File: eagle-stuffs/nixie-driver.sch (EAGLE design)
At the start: 65 parts, among them IC1 74141N/K155ID1, IC2 74LS595N, IC3 TPS562209, IC4 NE555, Q1 MPSA92, Q10 2N2222, Q11 IRF840, Q12 2N2222, Q2 MPSA92, Q3 MPSA92, Q4 MPSA92, Q5 MPSA42, Q6 MPSA42, Q7 MPSA42, Q8 MPSA42, Q9 PN2907

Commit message: Updated something
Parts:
- R11: value 27 -> 56
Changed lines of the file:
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@@
 <part name="R9" library="resistor" deviceset="R-US_" device="0207/10" value="10k"/>
 <part name="R10" library="resistor" deviceset="R-US_" device="0207/10" value="10k"/>
-<part name="R11" library="resistor" deviceset="R-US_" device="0207/10" value="27"/>
+<part name="R11" library="resistor" deviceset="R-US_" device="0207/10" value="56"/>
 <part name="R12" library="resistor" deviceset="R-US_" device="0207/10" value="10k"/>
 <part name="R13" library="resistor" deviceset="R-US_" device="0207/10" value="15k"/>

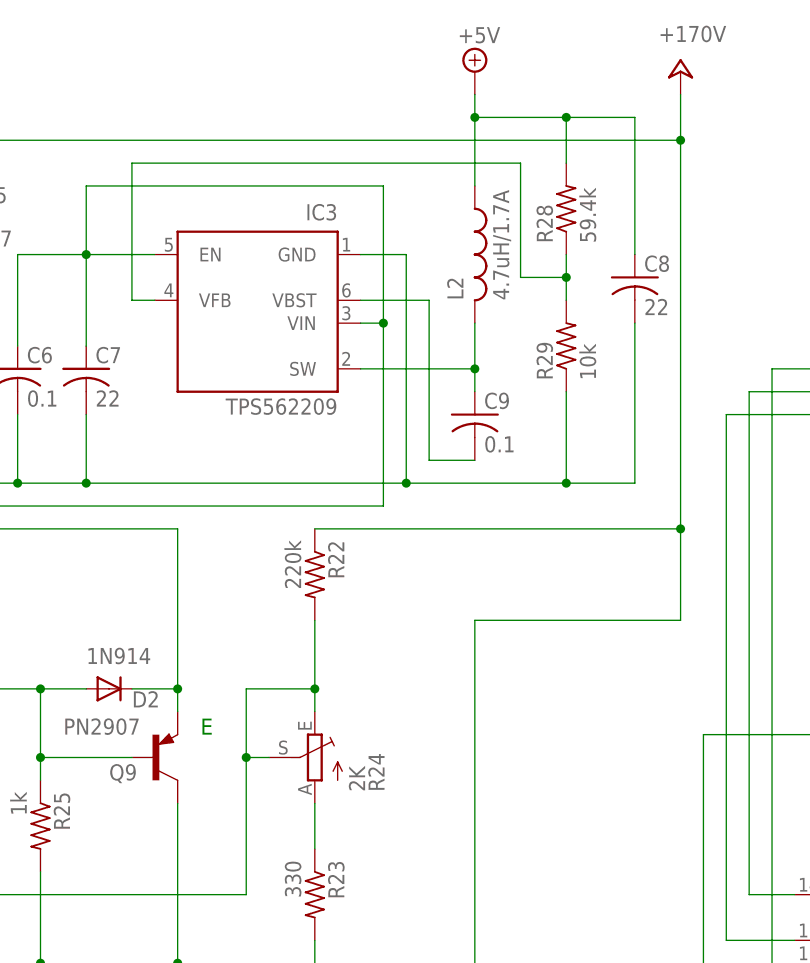
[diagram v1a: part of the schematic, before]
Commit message: Layout adjustement
Adjusted some physical component size & layout
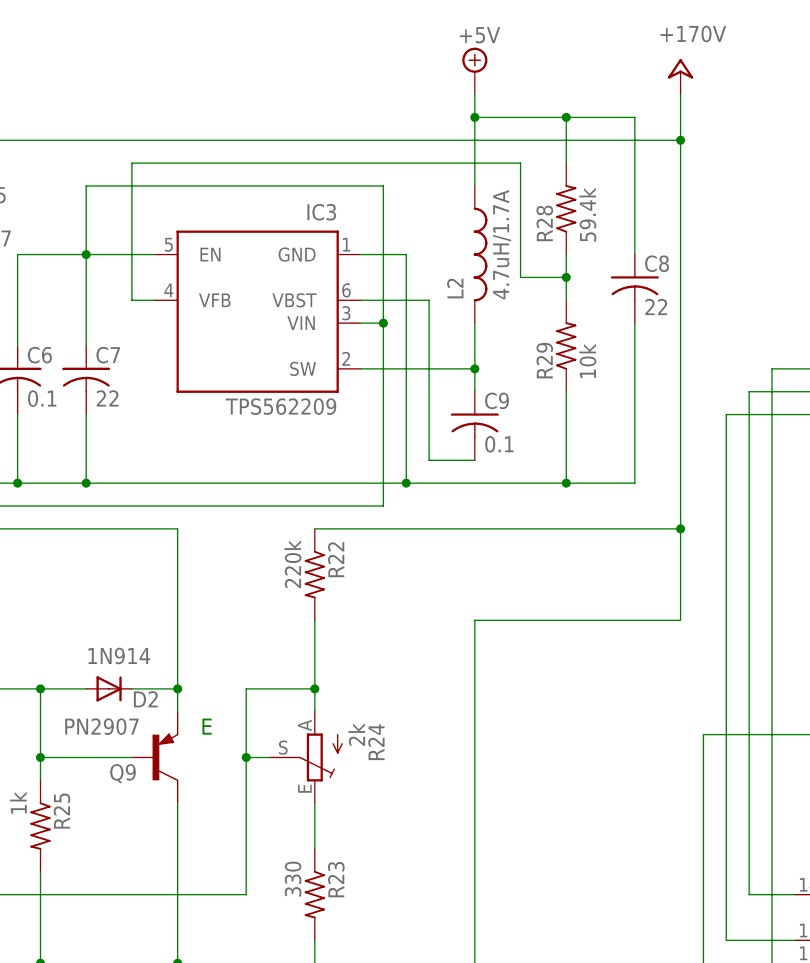
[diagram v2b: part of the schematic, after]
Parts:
- L2: device resistor:L-US0207/10 -> resistor:L-US0207/12
- R24: value 2K -> 2k; device pot:TRIM_EU-CT6 -> pot:TRIM_EU-CA6V
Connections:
- net N$64: now also R24.A; no longer R24.E
- net N$65: now also R24.E; no longer R24.A
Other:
- note added: "Capacitor value in uF in not noted, C4/C5 300v rated"
- note removed: "Capacitor value in uF in not noted"
- moved on the sheet: R24
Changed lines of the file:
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@@
 <part name="R22" library="resistor" deviceset="R-US_" device="0207/10" value="220k"/>
 <part name="R23" library="resistor" deviceset="R-US_" device="0207/10" value="330"/>
-<part name="R24" library="pot" deviceset="TRIM_EU-" device="CT6" value="2K"/>
 <part name="D2" library="diode" deviceset="1N4004" device="" value="1N914"/>
 <part name="Q9" library="transistor-pnp" deviceset="2N4126*" device="" value="PN2907"/>
@@
 <part name="IC3" library="texas" deviceset="TPS6107*" device="DDC" technology="0" value="TPS562209"/>
 <part name="R21" library="resistor" deviceset="R-US_" device="0207/10" value="2.2k"/>
-<part name="L2" library="resistor" deviceset="L-US" device="0207/10" value="4.7uH/1.7A"/>
 <part name="P+1" library="supply1" deviceset="+24V" device="" value="+170V"/>
 <part name="C1" library="rcl" deviceset="CPOL-US" device="E2,5-6E" value="100"/>
@@
 <part name="R29" library="resistor" deviceset="R-US_" device="0204/2V" value="10k"/>
 <part name="C6" library="rcl" deviceset="C-US" device="050-024X044" value="0.1"/>
+<part name="R24" library="pot" deviceset="TRIM_EU-" device="CA6V" value="2k"/>
+<part name="L2" library="resistor" deviceset="L-US" device="0207/12" value="4.7uH/1.7A"/>
 </parts>
 <sheets>
@@
 <wire x1="144.78" y1="99.06" x2="7.62" y2="99.06" width="0.1524" layer="98" style="shortdash"/>
 <wire x1="7.62" y1="99.06" x2="7.62" y2="203.2" width="0.1524" layer="98" style="shortdash"/>
-<text x="27.94" y="205.74" size="1.778" layer="98">Power supply (+5v / 500mA, +170v / 6 mA)</text>
+<text x="38.1" y="208.28" size="1.778" layer="98">Power supply (+5v / 500mA, +170v / 6 mA)</text>
 <text x="223.52" y="45.72" size="1.778" layer="98">Cathode drivers &amp; Ambient led</text>
 <wire x1="147.32" y1="134.62" x2="269.24" y2="134.62" width="0.1524" layer="98" style="shortdash"/>
@@
 <text x="175.26" y="25.4" size="2.54" layer="98" font="fixed">Project:</text>
 <text x="193.04" y="25.4" size="2.54" layer="98" font="fixed">Y.A.N.C. (Yet Another Nixie Clock)</text>
-<text x="83.82" y="200.66" size="1.778" layer="98">Capacitor value in uF in not noted</text>
+<text x="38.1" y="205.74" size="1.778" layer="98">Capacitor value in uF in not noted, C4/C5 300v rated</text>
 <text x="175.26" y="7.62" size="2.54" layer="98" font="fixed">Licensed under CERN OHL v.1.2 or later</text>
 </plain>
@@
 <attribute name="VALUE" x="118.618" y="118.11" size="1.778" layer="96" rot="R270"/>
 </instance>
-<instance part="R24" gate="1" x="121.92" y="129.54" smashed="yes" rot="MR0">
-<attribute name="NAME" x="127.889" y="125.73" size="1.778" layer="95" rot="MR90"/>
-<attribute name="VALUE" x="125.73" y="125.73" size="1.778" layer="96" rot="MR90"/>
-</instance>
 <instance part="D2" gate="1" x="99.06" y="137.16" smashed="yes">
 <attribute name="NAME" x="101.6" y="135.1026" size="1.778" layer="95"/>
@@
 <attribute name="NAME" x="57.3786" y="194.31" size="1.778" layer="95" rot="R270"/>
 <attribute name="VALUE" x="52.578" y="194.31" size="1.778" layer="96" rot="R270"/>
-</instance>
-<instance part="L2" gate="G$1" x="139.7" y="185.42" smashed="yes">
-<attribute name="NAME" x="138.43" y="180.34" size="1.778" layer="95" rot="R90"/>
-<attribute name="VALUE" x="143.51" y="180.34" size="1.778" layer="96" rot="R90"/>
 </instance>
 <instance part="P+1" gate="1" x="162.56" y="205.74" smashed="yes">
@@
 <instance part="R29" gate="G$1" x="149.86" y="175.26" rot="R90"/>
 <instance part="C6" gate="G$1" x="88.9" y="172.72"/>
+<instance part="R24" gate="1" x="121.92" y="129.54" rot="R180"/>
+<instance part="L2" gate="G$1" x="139.7" y="185.42"/>
 </instances>
 <busses>
@@
 <wire x1="149.86" y1="200.66" x2="149.86" y2="195.58" width="0.1524" layer="91"/>
 <junction x="139.7" y="200.66"/>
-<pinref part="L2" gate="G$1" pin="1"/>
 <wire x1="149.86" y1="200.66" x2="157.48" y2="200.66" width="0.1524" layer="91"/>
 <wire x1="157.48" y1="200.66" x2="157.48" y2="185.42" width="0.1524" layer="91"/>
@@
 <pinref part="C8" gate="G$1" pin="1"/>
 <pinref part="R28" gate="G$1" pin="2"/>
+<pinref part="L2" gate="G$1" pin="1"/>
 </segment>
 <segment>
@@
 <wire x1="73.66" y1="114.3" x2="114.3" y2="114.3" width="0.1524" layer="91"/>
 <wire x1="114.3" y1="114.3" x2="114.3" y2="129.54" width="0.1524" layer="91"/>
-<pinref part="R24" gate="1" pin="S"/>
 <wire x1="114.3" y1="129.54" x2="116.84" y2="129.54" width="0.1524" layer="91"/>
 <wire x1="114.3" y1="137.16" x2="114.3" y2="129.54" width="0.1524" layer="91"/>
 <junction x="114.3" y="129.54"/>
-<pinref part="R24" gate="1" pin="E"/>
 <pinref part="R22" gate="G$1" pin="2"/>
 <wire x1="121.92" y1="134.62" x2="121.92" y2="137.16" width="0.1524" layer="91"/>
@@
 <junction x="121.92" y="137.16"/>
 <pinref part="Q10" gate="G$1" pin="B"/>
+<pinref part="R24" gate="1" pin="A"/>
+<pinref part="R24" gate="1" pin="S"/>
 </segment>
 </net>
 <net name="N$65" class="0">
 <segment>
-<pinref part="R24" gate="1" pin="A"/>
 <pinref part="R23" gate="G$1" pin="1"/>
 <wire x1="121.92" y1="119.38" x2="121.92" y2="124.46" width="0.1524" layer="91"/>
+<pinref part="R24" gate="1" pin="E"/>
 </segment>
 </net>
@@
 <net name="SW" class="0">
 <segment>
-<pinref part="L2" gate="G$1" pin="2"/>
 <pinref part="C9" gate="G$1" pin="1"/>
 <wire x1="139.7" y1="170.18" x2="139.7" y2="172.72" width="0.1524" layer="91"/>
@@
 <wire x1="127" y1="172.72" x2="139.7" y2="172.72" width="0.1524" layer="91"/>
 <junction x="139.7" y="172.72"/>
-</segment>
-</net>
+<pinref part="L2" gate="G$1" pin="2"/>
+</segment>
+</net>

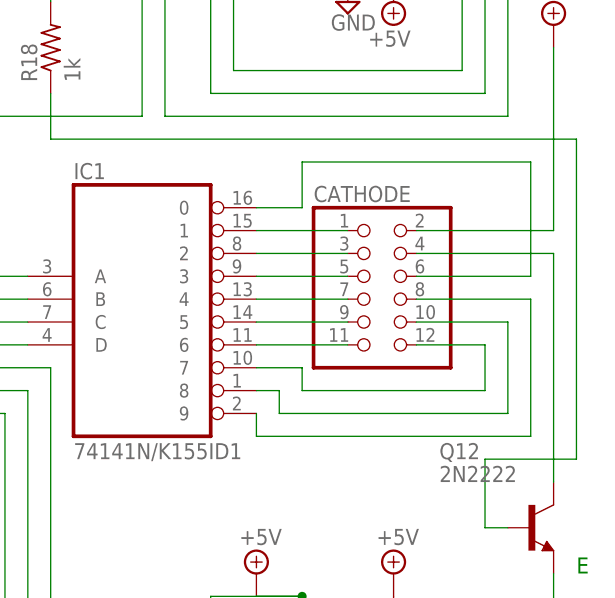
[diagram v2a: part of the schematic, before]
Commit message: Mirror cathod connector
Corrected major layout error!!! Needed to mirror cathod connector since
it mounted on bottom layer on lamp board and not on this board. Blowed
up my Pi this morning for the maiden test of the board :-(
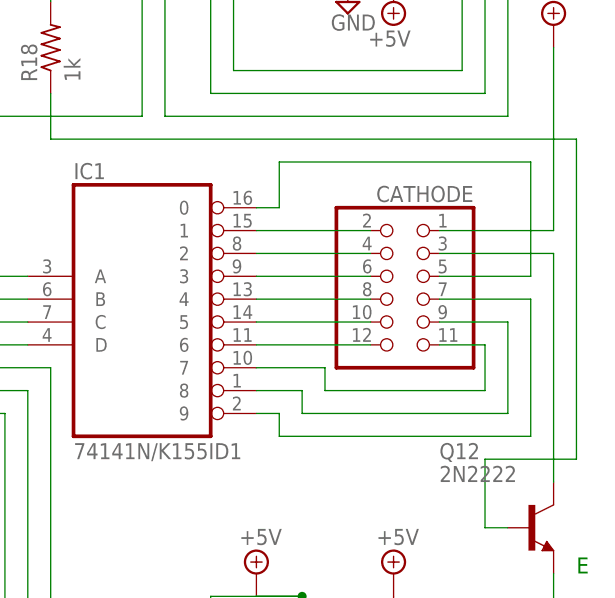
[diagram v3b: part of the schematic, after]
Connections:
- net +5V: now also CATHODE.1; no longer CATHODE.2
- net N$10: now also CATHODE.7; no longer CATHODE.8
- net N$11: now also CATHODE.5; no longer CATHODE.6
- net N$2: now also CATHODE.2; no longer CATHODE.1
- net N$3: now also CATHODE.4; no longer CATHODE.3
- net N$4: now also CATHODE.6; no longer CATHODE.5
- net N$45: now also CATHODE.3; no longer CATHODE.4
- net N$5: now also CATHODE.8; no longer CATHODE.7
- net N$6: now also CATHODE.10; no longer CATHODE.9
- net N$7: now also CATHODE.12; no longer CATHODE.11
- net N$8: now also CATHODE.11; no longer CATHODE.12
- net N$9: now also CATHODE.9; no longer CATHODE.10
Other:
- moved on the sheet: CATHODE
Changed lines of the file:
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@@
 <instance part="SUPPLY8" gate="+5V" x="231.14" y="81.28"/>
 <instance part="SUPPLY9" gate="+5V" x="246.38" y="81.28"/>
-<instance part="CATHODE" gate="A" x="243.84" y="114.3"/>
+<instance part="CATHODE" gate="A" x="248.92" y="114.3" rot="MR0"/>
 <instance part="PI" gate="A" x="223.52" y="157.48" rot="R270"/>
 <instance part="SUPPLY10" gate="GND" x="264.16" y="55.88"/>
@@
 </segment>
 <segment>
-<pinref part="CATHODE" gate="A" pin="2"/>
-<wire x1="248.92" y1="119.38" x2="264.16" y2="119.38" width="0.1524" layer="91"/>
 <pinref part="SUPPLY14" gate="+5V" pin="+5V"/>
 <wire x1="264.16" y1="139.7" x2="264.16" y2="119.38" width="0.1524" layer="91"/>
+<pinref part="CATHODE" gate="A" pin="1"/>
+<wire x1="264.16" y1="119.38" x2="251.46" y2="119.38" width="0.1524" layer="91"/>
 </segment>
 <segment>
@@
 </segment>
 </net>
-<net name="N$2" class="0">
-<segment>
-<pinref part="IC1" gate="A" pin="1"/>
-<pinref part="CATHODE" gate="A" pin="1"/>
-<wire x1="231.14" y1="119.38" x2="241.3" y2="119.38" width="0.1524" layer="91"/>
-</segment>
-</net>
-<net name="N$3" class="0">
-<segment>
-<pinref part="IC1" gate="A" pin="2"/>
-<pinref part="CATHODE" gate="A" pin="3"/>
-<wire x1="231.14" y1="116.84" x2="241.3" y2="116.84" width="0.1524" layer="91"/>
-</segment>
-</net>
-<net name="N$4" class="0">
-<segment>
-<pinref part="IC1" gate="A" pin="3"/>
-<pinref part="CATHODE" gate="A" pin="5"/>
-<wire x1="231.14" y1="114.3" x2="241.3" y2="114.3" width="0.1524" layer="91"/>
-</segment>
-</net>
-<net name="N$5" class="0">
-<segment>
-<pinref part="IC1" gate="A" pin="4"/>
-<pinref part="CATHODE" gate="A" pin="7"/>
-<wire x1="231.14" y1="111.76" x2="241.3" y2="111.76" width="0.1524" layer="91"/>
-</segment>
-</net>
-<net name="N$6" class="0">
-<segment>
-<pinref part="IC1" gate="A" pin="5"/>
-<pinref part="CATHODE" gate="A" pin="9"/>
-<wire x1="231.14" y1="109.22" x2="241.3" y2="109.22" width="0.1524" layer="91"/>
-</segment>
-</net>
-<net name="N$7" class="0">
-<segment>
-<pinref part="IC1" gate="A" pin="6"/>
-<pinref part="CATHODE" gate="A" pin="11"/>
-<wire x1="231.14" y1="106.68" x2="241.3" y2="106.68" width="0.1524" layer="91"/>
-</segment>
-</net>
-<net name="N$8" class="0">
-<segment>
-<pinref part="IC1" gate="A" pin="7"/>
-<wire x1="231.14" y1="104.14" x2="236.22" y2="104.14" width="0.1524" layer="91"/>
-<wire x1="236.22" y1="104.14" x2="236.22" y2="101.6" width="0.1524" layer="91"/>
-<wire x1="236.22" y1="101.6" x2="256.54" y2="101.6" width="0.1524" layer="91"/>
-<wire x1="256.54" y1="101.6" x2="256.54" y2="106.68" width="0.1524" layer="91"/>
-<pinref part="CATHODE" gate="A" pin="12"/>
-<wire x1="256.54" y1="106.68" x2="248.92" y2="106.68" width="0.1524" layer="91"/>
-</segment>
-</net>
-<net name="N$9" class="0">
-<segment>
-<pinref part="IC1" gate="A" pin="8"/>
-<wire x1="231.14" y1="101.6" x2="233.68" y2="101.6" width="0.1524" layer="91"/>
-<wire x1="233.68" y1="101.6" x2="233.68" y2="99.06" width="0.1524" layer="91"/>
-<wire x1="233.68" y1="99.06" x2="259.08" y2="99.06" width="0.1524" layer="91"/>
-<wire x1="259.08" y1="99.06" x2="259.08" y2="109.22" width="0.1524" layer="91"/>
-<pinref part="CATHODE" gate="A" pin="10"/>
-<wire x1="259.08" y1="109.22" x2="248.92" y2="109.22" width="0.1524" layer="91"/>
-</segment>
-</net>
-<net name="N$10" class="0">
-<segment>
-<pinref part="IC1" gate="A" pin="9"/>
-<wire x1="231.14" y1="99.06" x2="231.14" y2="96.52" width="0.1524" layer="91"/>
-<wire x1="231.14" y1="96.52" x2="261.62" y2="96.52" width="0.1524" layer="91"/>
-<wire x1="261.62" y1="96.52" x2="261.62" y2="111.76" width="0.1524" layer="91"/>
-<pinref part="CATHODE" gate="A" pin="8"/>
-<wire x1="261.62" y1="111.76" x2="248.92" y2="111.76" width="0.1524" layer="91"/>
-</segment>
-</net>
-<net name="N$11" class="0">
-<segment>
-<pinref part="IC1" gate="A" pin="0"/>
-<wire x1="231.14" y1="121.92" x2="236.22" y2="121.92" width="0.1524" layer="91"/>
-<wire x1="236.22" y1="121.92" x2="236.22" y2="127" width="0.1524" layer="91"/>
-<wire x1="236.22" y1="127" x2="261.62" y2="127" width="0.1524" layer="91"/>
-<wire x1="261.62" y1="127" x2="261.62" y2="114.3" width="0.1524" layer="91"/>
-<pinref part="CATHODE" gate="A" pin="6"/>
-<wire x1="261.62" y1="114.3" x2="248.92" y2="114.3" width="0.1524" layer="91"/>
-</segment>
-</net>
 <net name="N$41" class="0">
 <segment>
@@
 <net name="N$45" class="0">
 <segment>
-<pinref part="CATHODE" gate="A" pin="4"/>
-<wire x1="248.92" y1="116.84" x2="264.16" y2="116.84" width="0.1524" layer="91"/>
 <wire x1="264.16" y1="116.84" x2="264.16" y2="91.44" width="0.1524" layer="91"/>
 <pinref part="Q12" gate="G$1" pin="C"/>
+<pinref part="CATHODE" gate="A" pin="3"/>
+<wire x1="264.16" y1="116.84" x2="251.46" y2="116.84" width="0.1524" layer="91"/>
 </segment>
 </net>
@@
 </segment>
 </net>
+<net name="N$2" class="0">
+<segment>
+<pinref part="IC1" gate="A" pin="1"/>
+<pinref part="CATHODE" gate="A" pin="2"/>
+<wire x1="231.14" y1="119.38" x2="243.84" y2="119.38" width="0.1524" layer="91"/>
+</segment>
+</net>
+<net name="N$3" class="0">
+<segment>
+<pinref part="IC1" gate="A" pin="2"/>
+<pinref part="CATHODE" gate="A" pin="4"/>
+<wire x1="231.14" y1="116.84" x2="243.84" y2="116.84" width="0.1524" layer="91"/>
+</segment>
+</net>
+<net name="N$4" class="0">
+<segment>
+<pinref part="IC1" gate="A" pin="3"/>
+<pinref part="CATHODE" gate="A" pin="6"/>
+<wire x1="231.14" y1="114.3" x2="243.84" y2="114.3" width="0.1524" layer="91"/>
+</segment>
+</net>
+<net name="N$5" class="0">
+<segment>
+<pinref part="IC1" gate="A" pin="4"/>
+<pinref part="CATHODE" gate="A" pin="8"/>
+<wire x1="231.14" y1="111.76" x2="243.84" y2="111.76" width="0.1524" layer="91"/>
+</segment>
+</net>
+<net name="N$6" class="0">
+<segment>
+<pinref part="IC1" gate="A" pin="5"/>
+<pinref part="CATHODE" gate="A" pin="10"/>
+<wire x1="231.14" y1="109.22" x2="243.84" y2="109.22" width="0.1524" layer="91"/>
+</segment>
+</net>
+<net name="N$7" class="0">
+<segment>
+<pinref part="IC1" gate="A" pin="6"/>
+<pinref part="CATHODE" gate="A" pin="12"/>
+<wire x1="231.14" y1="106.68" x2="243.84" y2="106.68" width="0.1524" layer="91"/>
+</segment>
+</net>
+<net name="N$8" class="0">
+<segment>
+<pinref part="CATHODE" gate="A" pin="11"/>
+<wire x1="251.46" y1="106.68" x2="256.54" y2="106.68" width="0.1524" layer="91"/>
+<wire x1="256.54" y1="106.68" x2="256.54" y2="101.6" width="0.1524" layer="91"/>
+<wire x1="256.54" y1="101.6" x2="238.76" y2="101.6" width="0.1524" layer="91"/>
+<wire x1="238.76" y1="101.6" x2="238.76" y2="104.14" width="0.1524" layer="91"/>
+<pinref part="IC1" gate="A" pin="7"/>
+<wire x1="238.76" y1="104.14" x2="231.14" y2="104.14" width="0.1524" layer="91"/>
+</segment>
+</net>
+<net name="N$9" class="0">
+<segment>
+<pinref part="IC1" gate="A" pin="8"/>
+<wire x1="231.14" y1="101.6" x2="236.22" y2="101.6" width="0.1524" layer="91"/>
+<wire x1="236.22" y1="101.6" x2="236.22" y2="99.06" width="0.1524" layer="91"/>
+<wire x1="236.22" y1="99.06" x2="259.08" y2="99.06" width="0.1524" layer="91"/>
+<wire x1="259.08" y1="99.06" x2="259.08" y2="109.22" width="0.1524" layer="91"/>
+<pinref part="CATHODE" gate="A" pin="9"/>
+<wire x1="259.08" y1="109.22" x2="251.46" y2="109.22" width="0.1524" layer="91"/>
+</segment>
+</net>
+<net name="N$10" class="0">
+<segment>
+<pinref part="IC1" gate="A" pin="9"/>
+<wire x1="231.14" y1="99.06" x2="233.68" y2="99.06" width="0.1524" layer="91"/>
+<wire x1="233.68" y1="99.06" x2="233.68" y2="96.52" width="0.1524" layer="91"/>
+<wire x1="233.68" y1="96.52" x2="261.62" y2="96.52" width="0.1524" layer="91"/>
+<wire x1="261.62" y1="96.52" x2="261.62" y2="111.76" width="0.1524" layer="91"/>
+<pinref part="CATHODE" gate="A" pin="7"/>
+<wire x1="261.62" y1="111.76" x2="251.46" y2="111.76" width="0.1524" layer="91"/>
+</segment>
+</net>
+<net name="N$11" class="0">
+<segment>
+<pinref part="CATHODE" gate="A" pin="5"/>
+<wire x1="251.46" y1="114.3" x2="261.62" y2="114.3" width="0.1524" layer="91"/>
+<wire x1="261.62" y1="114.3" x2="261.62" y2="127" width="0.1524" layer="91"/>
+<wire x1="261.62" y1="127" x2="233.68" y2="127" width="0.1524" layer="91"/>
+<wire x1="233.68" y1="127" x2="233.68" y2="121.92" width="0.1524" layer="91"/>
+<pinref part="IC1" gate="A" pin="0"/>
+<wire x1="233.68" y1="121.92" x2="231.14" y2="121.92" width="0.1524" layer="91"/>
+</segment>
+</net>
